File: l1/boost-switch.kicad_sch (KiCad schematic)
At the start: 9 parts

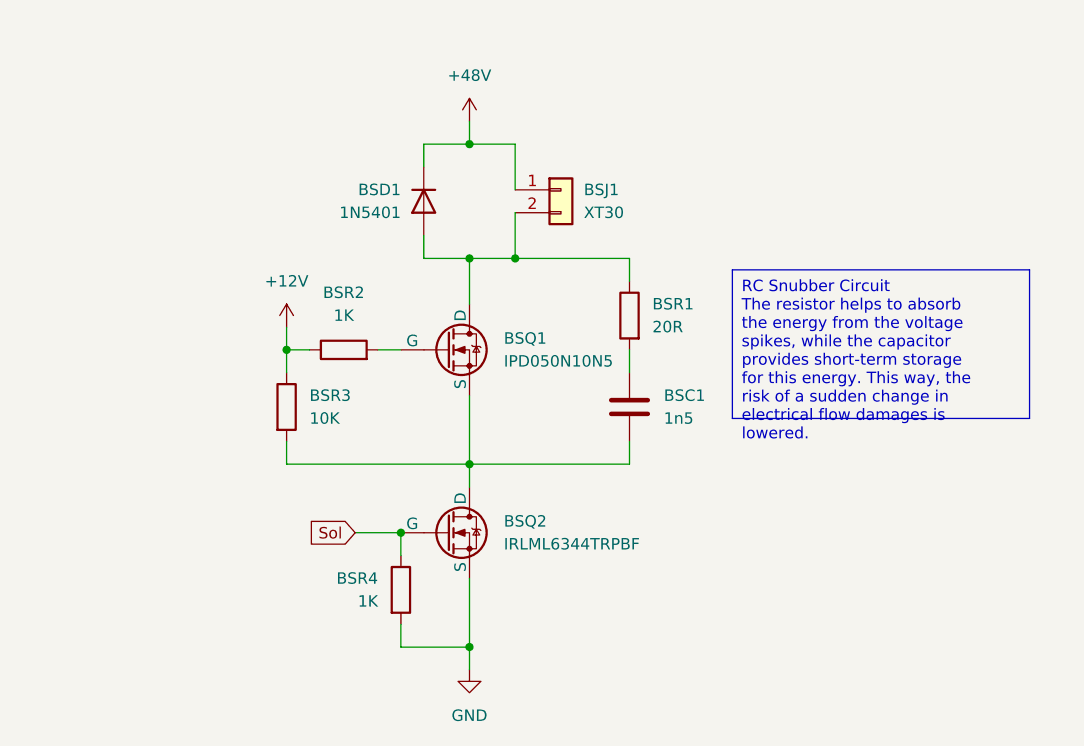
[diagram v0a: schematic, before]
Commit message: Changed To MOSFET Driver
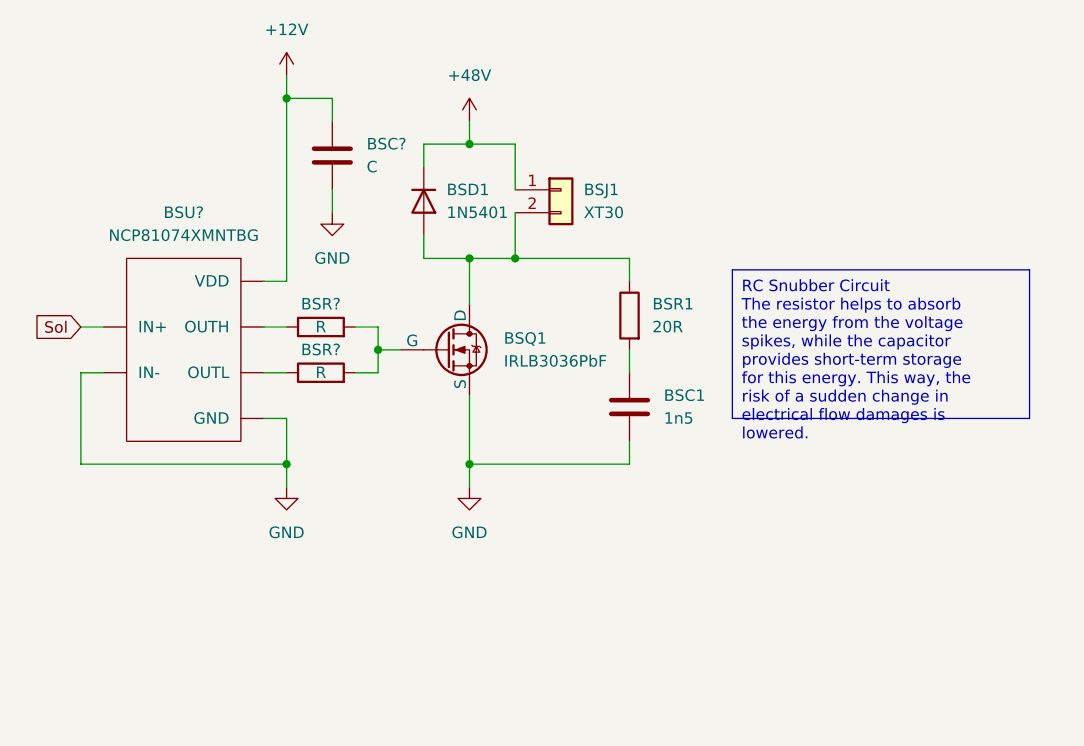
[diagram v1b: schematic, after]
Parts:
- removed BSQ2: IRLML6344TRPBF, Library:SOT95P237X112-3N, symbol vincent:IRLML6344TRPBF
- removed BSR2, BSR4: 1K, Library:res0603, symbol Device:R
- removed BSR3: 10K, Library:res0603, symbol Device:R
- added BSC?: C, symbol Device:C
- added BSR? (x2): R, symbol Device:R
- added BSU?: NCP81074XMNTBG, Library:SON50P200X200X100-9N, symbol senrobo_kicad:NCP81074XMNTBG
- BSQ1: value IPD050N10N5 -> IRLB3036PbF
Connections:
- net +12V: now also BSC?.1, BSU?.6 (VDD), BSU?.7 (VDD)
- net GND: now also BSC1.2, BSQ1.3 (S), BSC?.2, BSU?.2 (GND), BSU?.3 (GND), BSU?.8 (IN-), BSU?.9 (GND)
- net Sol: now also BSU?.1 (IN+)
- net at BSQ1.1 (G): now also BSR?.2, BSR?.2
- new net: BSR?.1, BSU?.4 (OUTL)
- new net: BSR?.1, BSU?.5 (OUTH)
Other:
- moved on the sheet: BSD1

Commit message: rough ideation
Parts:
- BSC1: renamed from BSC?; footprint (none) -> Library:res0603
- BSR2, BSR3: renamed from BSR?; footprint (none) -> Library:res0603
- gave numbers to parts that had none: 1
- renumbered BSC1 to BSC2
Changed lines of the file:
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@@
 		(on_board yes)
 		(dnp no)
-		(property "Reference" "BSC1"
+		(property "Reference" "BSC2"
 			(at 168.91 106.68 0)
 			(effects
@@
 			(project "l1"
 				(path "/0e4ddce5-5c0a-41d1-ab67-e7bad6d98362/f60e712f-1e16-44e9-aa12-ae1d10556a78"
-					(reference "BSC1")
+					(reference "BSC2")
 					(unit 1)
 				)
@@
 		(dnp no)
 		(fields_autoplaced yes)
-		(property "Reference" "#PWR075"
+		(property "Reference" "#PWR028"
 			(at 127 123.19 0)
 			(effects
@@
 			(project "l1"
 				(path "/0e4ddce5-5c0a-41d1-ab67-e7bad6d98362/f60e712f-1e16-44e9-aa12-ae1d10556a78"
-					(reference "#PWR075")
+					(reference "#PWR028")
 					(unit 1)
 				)
@@
 		(on_board yes)
 		(dnp no)
-		(property "Reference" "BSR?"
+		(property "Reference" "BSR3"
 			(at 130.81 101.6 90)
 			(effects
@@
 			)
 		)
-		(property "Footprint" ""
+		(property "Footprint" "Library:res0603"
 			(at 130.81 105.918 90)
 			(effects
@@
 			(project ""
 				(path "/0e4ddce5-5c0a-41d1-ab67-e7bad6d98362/f60e712f-1e16-44e9-aa12-ae1d10556a78"
-					(reference "BSR?")
+					(reference "BSR3")
 					(unit 1)
 				)
@@
 		(on_board yes)
 		(dnp no)
-		(property "Reference" "BSR?"
+		(property "Reference" "BSR2"
 			(at 130.81 96.52 90)
 			(effects
@@
 			)
 		)
-		(property "Footprint" ""
+		(property "Footprint" "Library:res0603"
 			(at 130.81 100.838 90)
 			(effects
@@
 			(project ""
 				(path "/0e4ddce5-5c0a-41d1-ab67-e7bad6d98362/f60e712f-1e16-44e9-aa12-ae1d10556a78"
-					(reference "BSR?")
+					(reference "BSR2")
 					(unit 1)
 				)
@@
 		(dnp no)
 		(fields_autoplaced yes)
-		(property "Reference" "#PWR034"
+		(property "Reference" "#PWR025"
 			(at 127 74.93 0)
 			(effects
@@
 			(project ""
 				(path "/0e4ddce5-5c0a-41d1-ab67-e7bad6d98362/f60e712f-1e16-44e9-aa12-ae1d10556a78"
-					(reference "#PWR034")
+					(reference "#PWR025")
 					(unit 1)
 				)
@@
 		(dnp no)
 		(fields_autoplaced yes)
-		(property "Reference" "BSC?"
+		(property "Reference" "BSC1"
 			(at 135.89 78.7399 0)
 			(effects
@@
 			)
 		)
-		(property "Footprint" ""
+		(property "Footprint" "Library:res0603"
 			(at 133.0452 83.82 0)
 			(effects
@@
 			(project ""
 				(path "/0e4ddce5-5c0a-41d1-ab67-e7bad6d98362/f60e712f-1e16-44e9-aa12-ae1d10556a78"
-					(reference "BSC?")
+					(reference "BSC1")
 					(unit 1)
 				)
@@
 		(dnp no)
 		(fields_autoplaced yes)
-		(property "Reference" "#PWR035"
+		(property "Reference" "#PWR029"
 			(at 147.32 123.19 0)
 			(effects
@@
 			(project "l1"
 				(path "/0e4ddce5-5c0a-41d1-ab67-e7bad6d98362/f60e712f-1e16-44e9-aa12-ae1d10556a78"
-					(reference "#PWR035")
+					(reference "#PWR029")
 					(unit 1)
 				)
@@
 		(dnp no)
 		(fields_autoplaced yes)
-		(property "Reference" "#PWR076"
+		(property "Reference" "#PWR027"
 			(at 132.08 92.71 0)
 			(effects
@@
 			(project ""
 				(path "/0e4ddce5-5c0a-41d1-ab67-e7bad6d98362/f60e712f-1e16-44e9-aa12-ae1d10556a78"
-					(reference "#PWR076")
+					(reference "#PWR027")
 					(unit 1)
 				)
@@
 		(dnp no)
 		(fields_autoplaced yes)
-		(property "Reference" "#PWR033"
+		(property "Reference" "#PWR026"
 			(at 147.32 80.01 0)
 			(effects
@@
 			(project "l1"
 				(path "/0e4ddce5-5c0a-41d1-ab67-e7bad6d98362/f60e712f-1e16-44e9-aa12-ae1d10556a78"
-					(reference "#PWR033")
+					(reference "#PWR026")
 					(unit 1)
 				)
@@
 		(dnp no)
 		(fields_autoplaced yes)
-		(property "Reference" "BSU?"
+		(property "Reference" "BSU1"
 			(at 115.57 86.36 0)
 			(effects
@@
 			(project ""
 				(path "/0e4ddce5-5c0a-41d1-ab67-e7bad6d98362/f60e712f-1e16-44e9-aa12-ae1d10556a78"
-					(reference "BSU?")
-					(unit 1)
-				)
+					(reference "BSU1")
+					(unit 1)
+				)
